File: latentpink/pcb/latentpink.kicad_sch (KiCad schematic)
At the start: 14 parts, among them M3 SCREWHOLE, M4 SCREWHOLE, M5 SCREWHOLE, M6 SCREWHOLE

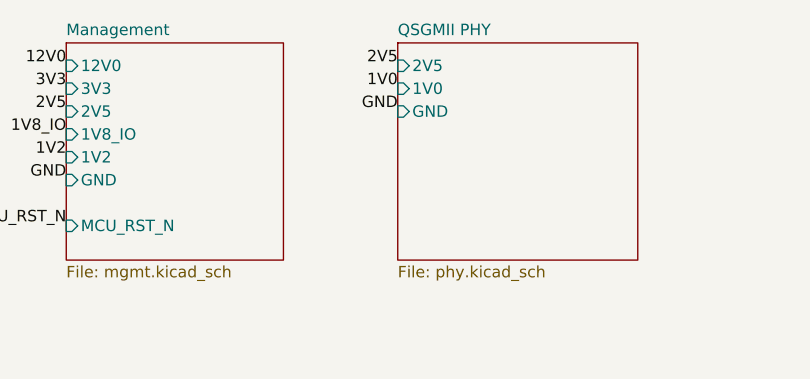
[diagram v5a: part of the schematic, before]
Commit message: Switched to new RJ45 for LATENTPINK, continued general PHY schematic
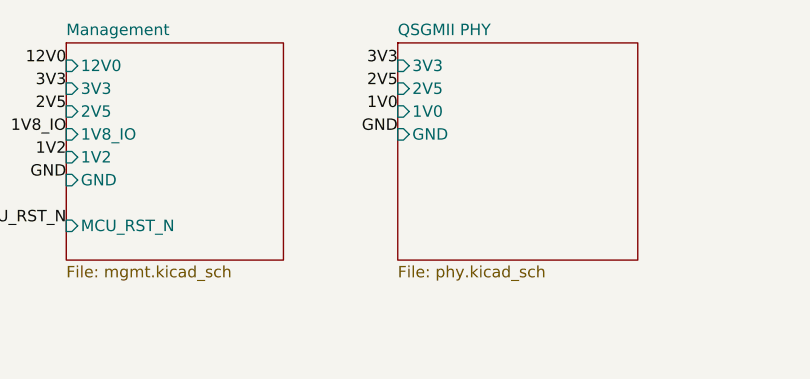
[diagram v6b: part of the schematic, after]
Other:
- sheet QSGMII PHY ports: added 3V3; removed none

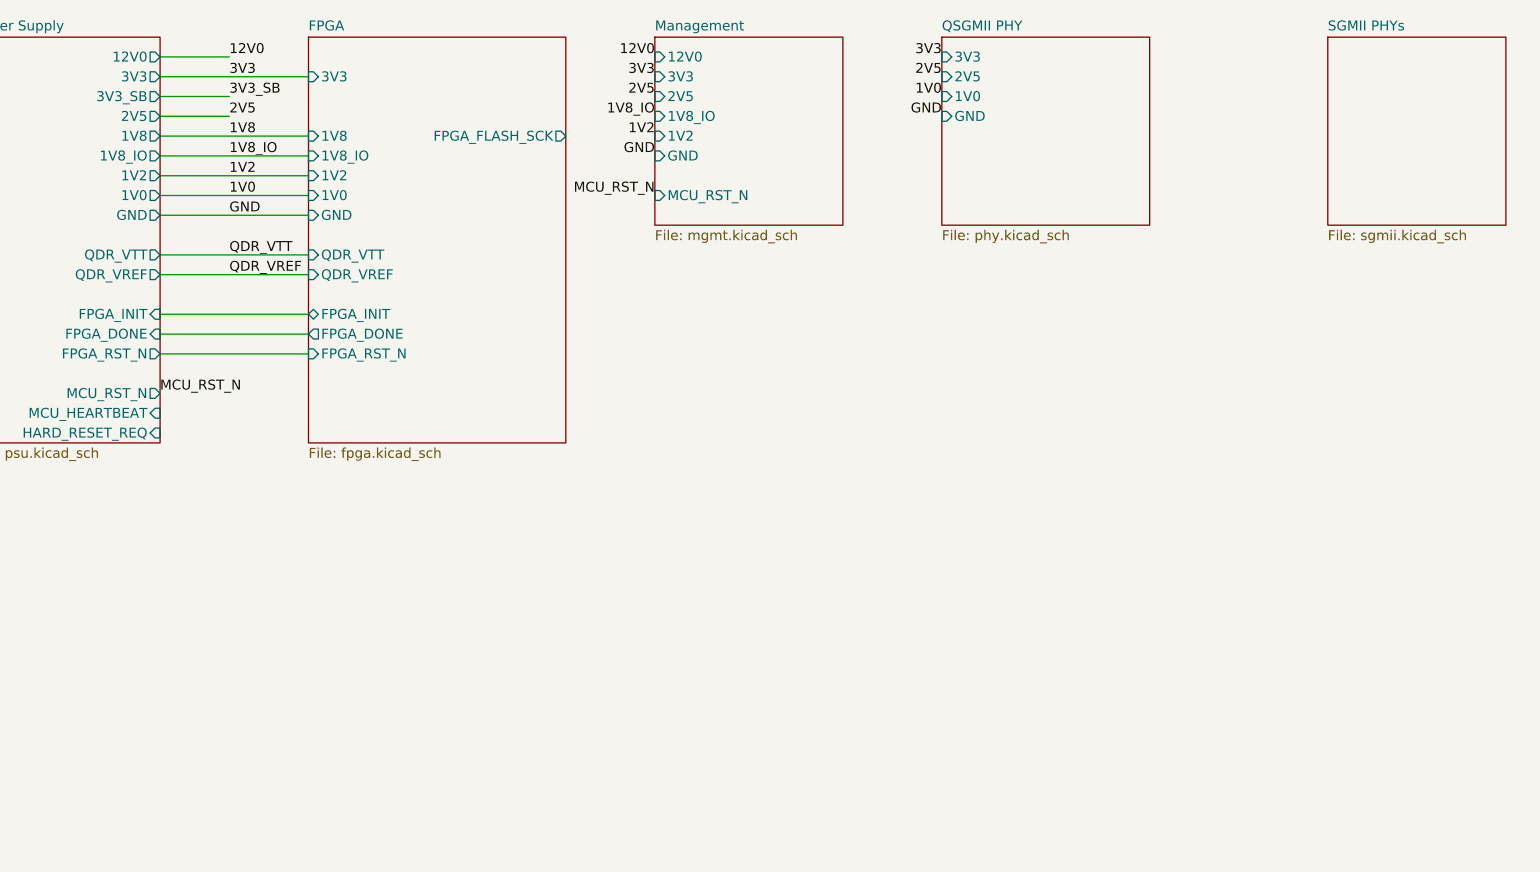
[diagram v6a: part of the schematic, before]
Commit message: Initial start of DP83867 schematic
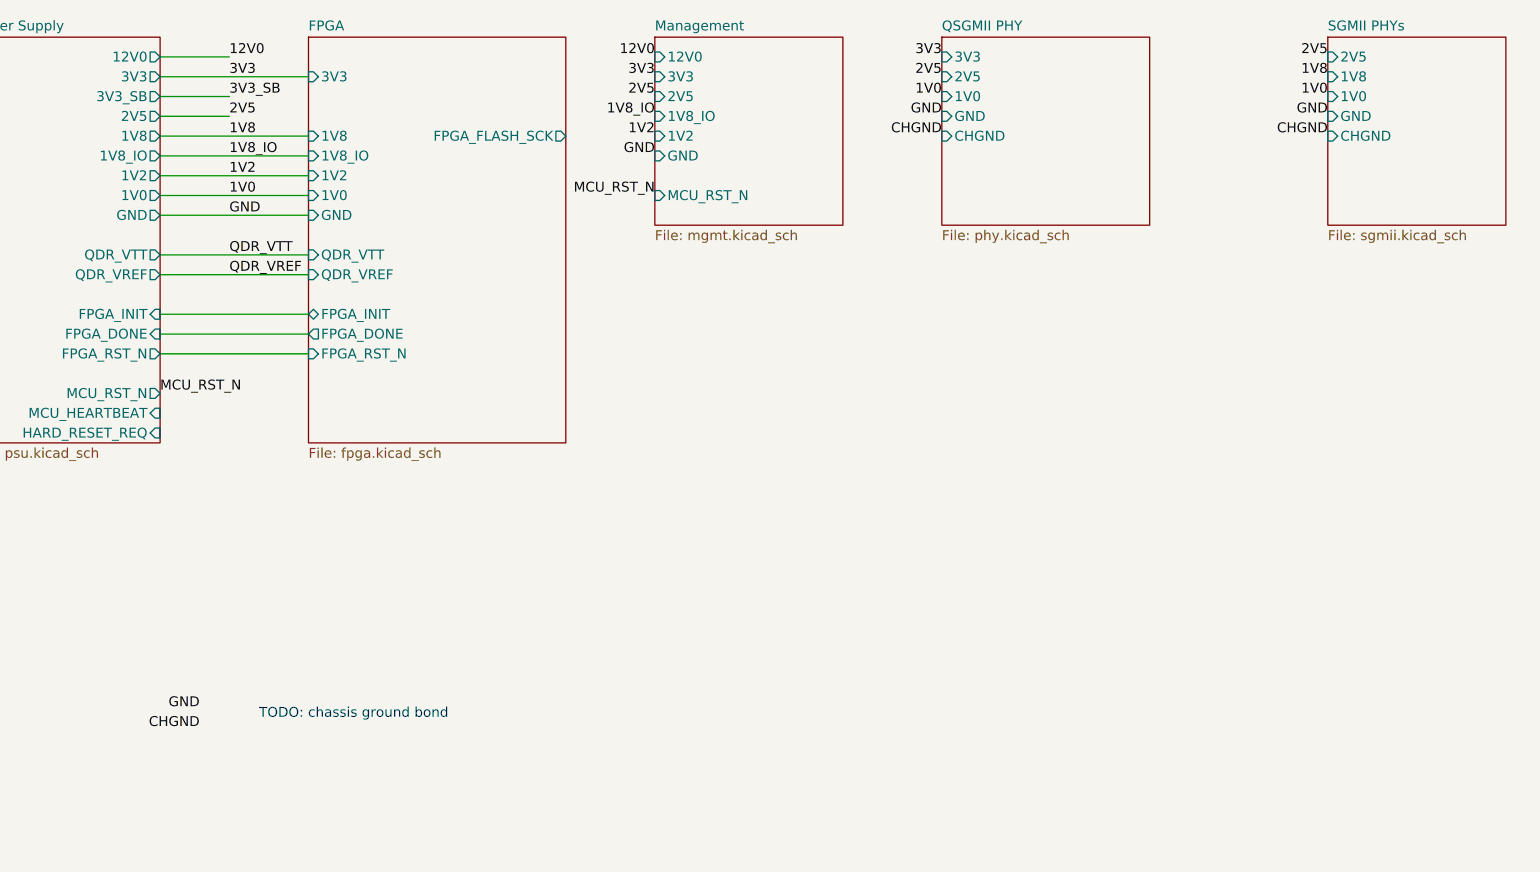
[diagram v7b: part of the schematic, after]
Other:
- sheet QSGMII PHY ports: added CHGND; removed none
- sheet SGMII PHYs ports: added 1V0, 1V8, 2V5, CHGND, GND; removed none
- note added: "TODO: chassis ground bond"
